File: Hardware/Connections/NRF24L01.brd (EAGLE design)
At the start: 34.3 x 28.9 mm, 9 parts

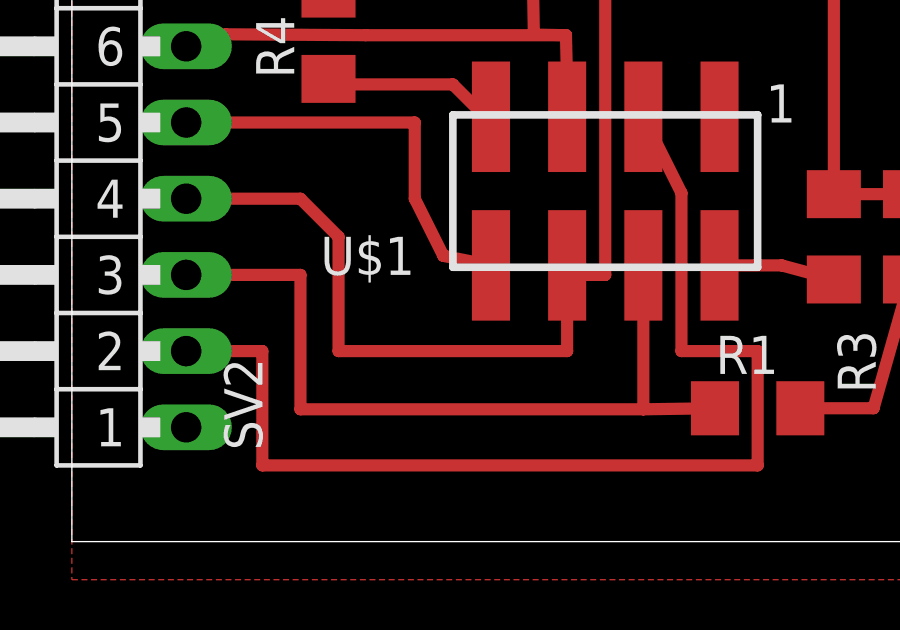
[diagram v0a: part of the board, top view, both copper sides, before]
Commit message: Updated PDF PCB files with Document outline mark. Fixed missing Name for NRF connector. Updated BOM to be correctly formatted.
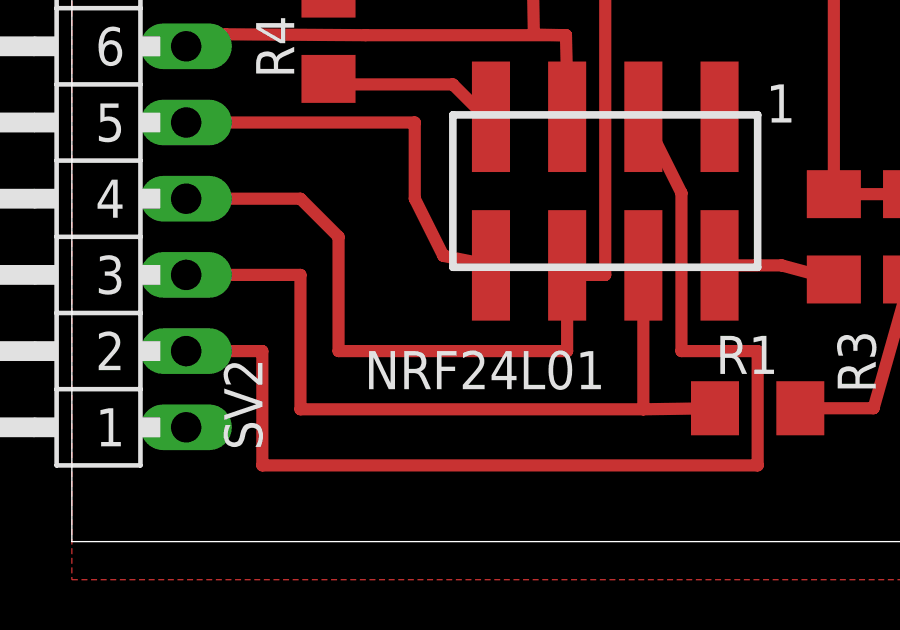
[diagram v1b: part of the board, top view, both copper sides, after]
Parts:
- renumbered U$1 to NRF24L01
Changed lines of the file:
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@@
 <grid distance="0.05" unitdist="inch" unit="mm" style="lines" multiple="1" display="no" altdistance="0.1" altunitdist="mm" altunit="mm"/>
 <layers>
-<layer number="1" name="Top" color="4" fill="1" visible="yes" active="yes"/>
+<layer number="1" name="Top" color="4" fill="1" visible="no" active="yes"/>
 <layer number="2" name="Route2" color="1" fill="3" visible="no" active="no"/>
 <layer number="3" name="Route3" color="4" fill="3" visible="no" active="no"/>
@@
 <layer number="14" name="Route14" color="1" fill="6" visible="no" active="no"/>
 <layer number="15" name="Route15" color="4" fill="6" visible="no" active="no"/>
-<layer number="16" name="Bottom" color="1" fill="1" visible="yes" active="yes"/>
-<layer number="17" name="Pads" color="2" fill="1" visible="yes" active="yes"/>
-<layer number="18" name="Vias" color="2" fill="1" visible="yes" active="yes"/>
-<layer number="19" name="Unrouted" color="6" fill="1" visible="yes" active="yes"/>
+<layer number="16" name="Bottom" color="1" fill="1" visible="no" active="yes"/>
+<layer number="17" name="Pads" color="2" fill="1" visible="no" active="yes"/>
+<layer number="18" name="Vias" color="2" fill="1" visible="no" active="yes"/>
+<layer number="19" name="Unrouted" color="6" fill="1" visible="no" active="yes"/>
 <layer number="20" name="Dimension" color="15" fill="1" visible="yes" active="yes"/>
 <layer number="21" name="tPlace" color="7" fill="1" visible="yes" active="yes"/>
 <layer number="22" name="bPlace" color="7" fill="1" visible="yes" active="yes"/>
-<layer number="23" name="tOrigins" color="15" fill="1" visible="yes" active="yes"/>
-<layer number="24" name="bOrigins" color="15" fill="1" visible="yes" active="yes"/>
+<layer number="23" name="tOrigins" color="15" fill="1" visible="no" active="yes"/>
+<layer number="24" name="bOrigins" color="15" fill="1" visible="no" active="yes"/>
 <layer number="25" name="tNames" color="7" fill="1" visible="yes" active="yes"/>
 <layer number="26" name="bNames" color="7" fill="1" visible="yes" active="yes"/>
 <layer number="27" name="tValues" color="7" fill="1" visible="no" active="yes"/>
 <layer number="28" name="bValues" color="7" fill="1" visible="no" active="yes"/>
-<layer number="29" name="tStop" color="7" fill="3" visible="yes" active="yes"/>
-<layer number="30" name="bStop" color="7" fill="6" visible="yes" active="yes"/>
-<layer number="31" name="tCream" color="7" fill="4" visible="yes" active="yes"/>
-<layer number="32" name="bCream" color="7" fill="5" visible="yes" active="yes"/>
-<layer number="33" name="tFinish" color="6" fill="3" visible="yes" active="yes"/>
-<layer number="34" name="bFinish" color="6" fill="6" visible="yes" active="yes"/>
-<layer number="35" name="tGlue" color="7" fill="4" visible="yes" active="yes"/>
-<layer number="36" name="bGlue" color="7" fill="5" visible="yes" active="yes"/>
-<layer number="37" name="tTest" color="7" fill="1" visible="yes" active="yes"/>
-<layer number="38" name="bTest" color="7" fill="1" visible="yes" active="yes"/>
-<layer number="39" name="tKeepout" color="4" fill="11" visible="yes" active="yes"/>
-<layer number="40" name="bKeepout" color="1" fill="11" visible="yes" active="yes"/>
-<layer number="41" name="tRestrict" color="4" fill="10" visible="yes" active="yes"/>
-<layer number="42" name="bRestrict" color="1" fill="10" visible="yes" active="yes"/>
-<layer number="43" name="vRestrict" color="2" fill="10" visible="yes" active="yes"/>
-<layer number="44" name="Drills" color="7" fill="1" visible="yes" active="yes"/>
-<layer number="45" name="Holes" color="7" fill="1" visible="yes" active="yes"/>
-<layer number="46" name="Milling" color="3" fill="1" visible="yes" active="yes"/>
-<layer number="47" name="Measures" color="7" fill="1" visible="yes" active="yes"/>
-<layer number="48" name="Document" color="7" fill="1" visible="yes" active="yes"/>
-<layer number="49" name="Reference" color="7" fill="1" visible="yes" active="yes"/>
+<layer number="29" name="tStop" color="7" fill="3" visible="no" active="yes"/>
+<layer number="30" name="bStop" color="7" fill="6" visible="no" active="yes"/>
+<layer number="31" name="tCream" color="7" fill="4" visible="no" active="yes"/>
+<layer number="32" name="bCream" color="7" fill="5" visible="no" active="yes"/>
+<layer number="33" name="tFinish" color="6" fill="3" visible="no" active="yes"/>
+<layer number="34" name="bFinish" color="6" fill="6" visible="no" active="yes"/>
+<layer number="35" name="tGlue" color="7" fill="4" visible="no" active="yes"/>
+<layer number="36" name="bGlue" color="7" fill="5" visible="no" active="yes"/>
+<layer number="37" name="tTest" color="7" fill="1" visible="no" active="yes"/>
+<layer number="38" name="bTest" color="7" fill="1" visible="no" active="yes"/>
+<layer number="39" name="tKeepout" color="4" fill="11" visible="no" active="yes"/>
+<layer number="40" name="bKeepout" color="1" fill="11" visible="no" active="yes"/>
+<layer number="41" name="tRestrict" color="4" fill="10" visible="no" active="yes"/>
+<layer number="42" name="bRestrict" color="1" fill="10" visible="no" active="yes"/>
+<layer number="43" name="vRestrict" color="2" fill="10" visible="no" active="yes"/>
+<layer number="44" name="Drills" color="7" fill="1" visible="no" active="yes"/>
+<layer number="45" name="Holes" color="7" fill="1" visible="no" active="yes"/>
+<layer number="46" name="Milling" color="3" fill="1" visible="no" active="yes"/>
+<layer number="47" name="Measures" color="7" fill="1" visible="no" active="yes"/>
+<layer number="48" name="Document" color="7" fill="1" visible="no" active="yes"/>
+<layer number="49" name="Reference" color="7" fill="1" visible="no" active="yes"/>
 <layer number="51" name="tDocu" color="7" fill="1" visible="yes" active="yes"/>
 <layer number="52" name="bDocu" color="7" fill="1" visible="yes" active="yes"/>
@@
 </element>
 <element name="EEPROM" library="eeprom" package="SO8" value="BR25S640FJ-WE2" x="15.24" y="21.59" rot="R270"/>
-<element name="U$1" library="Header" package="TSM-110-XX-XXX-DV" value="2X4SMDHEADER" x="17.78" y="11.43" rot="R180"/>
+<element name="NRF24L01" library="Header" package="TSM-110-XX-XXX-DV" value="2X4SMDHEADER" x="17.78" y="11.43" smashed="yes" rot="R180">
+<attribute name="NAME" x="17.78" y="6.35" size="1.27" layer="25" rot="R180"/>
+<attribute name="VALUE" x="11.43" y="13.97" size="1.27" layer="27" rot="R180"/>
+</element>
 <element name="R1" library="resistor" package="R1206" value="10K" x="22.86" y="4.445"/>
 <element name="R2" library="resistor" package="R1206" value="10K" x="7.62" y="24.765" smashed="yes" rot="R90">
@@
 <signal name="GND">
 <contactref element="SV2" pad="1"/>
-<contactref element="U$1" pad="1"/>
+<contactref element="NRF24L01" pad="1"/>
 <polygon width="0.4064" layer="1" isolate="0.4064">
 <vertex x="0" y="27.94"/>
@@
 <signal name="MOSI">
 <contactref element="EEPROM" pad="5"/>
-<contactref element="U$1" pad="6"/>
+<contactref element="NRF24L01" pad="6"/>
 <wire x1="17.78" y1="19.625" x2="17.84" y2="19.685" width="0.4064" layer="1"/>
 <contactref element="SV2" pad="4"/>
@@
 <signal name="SCK">
 <contactref element="EEPROM" pad="6"/>
-<contactref element="U$1" pad="5"/>
+<contactref element="NRF24L01" pad="5"/>
 <wire x1="16.47" y1="16.88" x2="15.4" y2="16.9" width="0.4064" layer="1"/>
 <wire x1="15.4" y1="16.9" x2="15.34" y2="20.385" width="0.4064" layer="1"/>
@@
 <signal name="CSN_RAD">
 <contactref element="R1" pad="1"/>
-<contactref element="U$1" pad="4"/>
+<contactref element="NRF24L01" pad="4"/>
 <contactref element="SV2" pad="3"/>
 <wire x1="19.05" y1="9.2075" x2="19.05" y2="4.41" width="0.4064" layer="1"/>
@@
 </signal>
 <signal name="CE_RAD">
-<contactref element="U$1" pad="3"/>
+<contactref element="NRF24L01" pad="3"/>
 <contactref element="SV2" pad="2"/>
 <wire x1="3.81" y1="6.35" x2="6.35" y2="6.35" width="0.4064" layer="1"/>
@@
 </signal>
 <signal name="IRQ_RAD">
-<contactref element="U$1" pad="8"/>
+<contactref element="NRF24L01" pad="8"/>
 <contactref element="SV2" pad="5"/>
 <wire x1="3.81" y1="13.97" x2="11.43" y2="13.97" width="0.4064" layer="1"/>
@@
 <signal name="N$2">
 <contactref element="R4" pad="1"/>
-<contactref element="U$1" pad="7"/>
+<contactref element="NRF24L01" pad="7"/>
 <wire x1="13.97" y1="14.1605" x2="13.7795" y2="14.1605" width="0.4064" layer="1"/>
 <wire x1="13.7795" y1="14.1605" x2="12.7" y2="15.24" width="0.4064" layer="1"/>
@@
 </signal>
 <signal name="N$1">
-<contactref element="U$1" pad="2"/>
+<contactref element="NRF24L01" pad="2"/>
 <contactref element="R3" pad="1"/>
 <wire x1="25.4" y1="8.738" x2="23.6605" y2="9.2075" width="0.4064" layer="1"/>

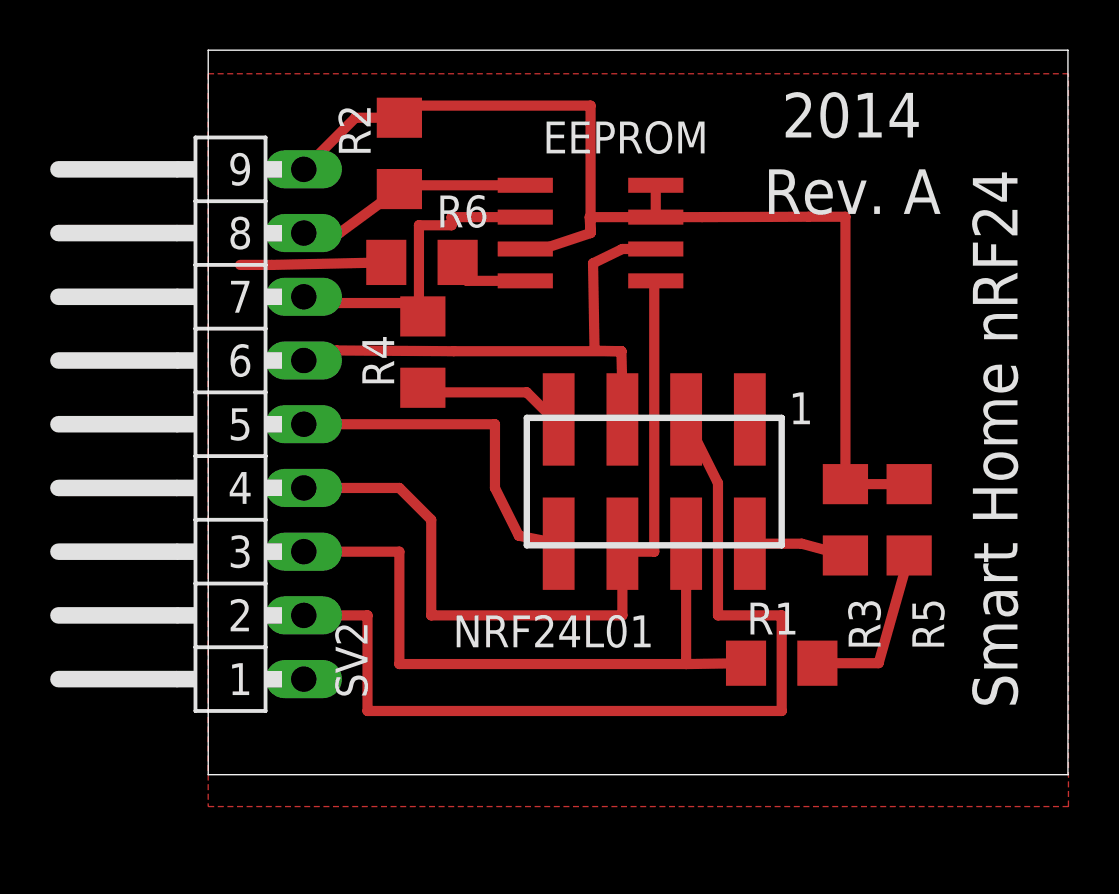
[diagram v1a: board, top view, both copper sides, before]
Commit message: updated pcb design to have reference points
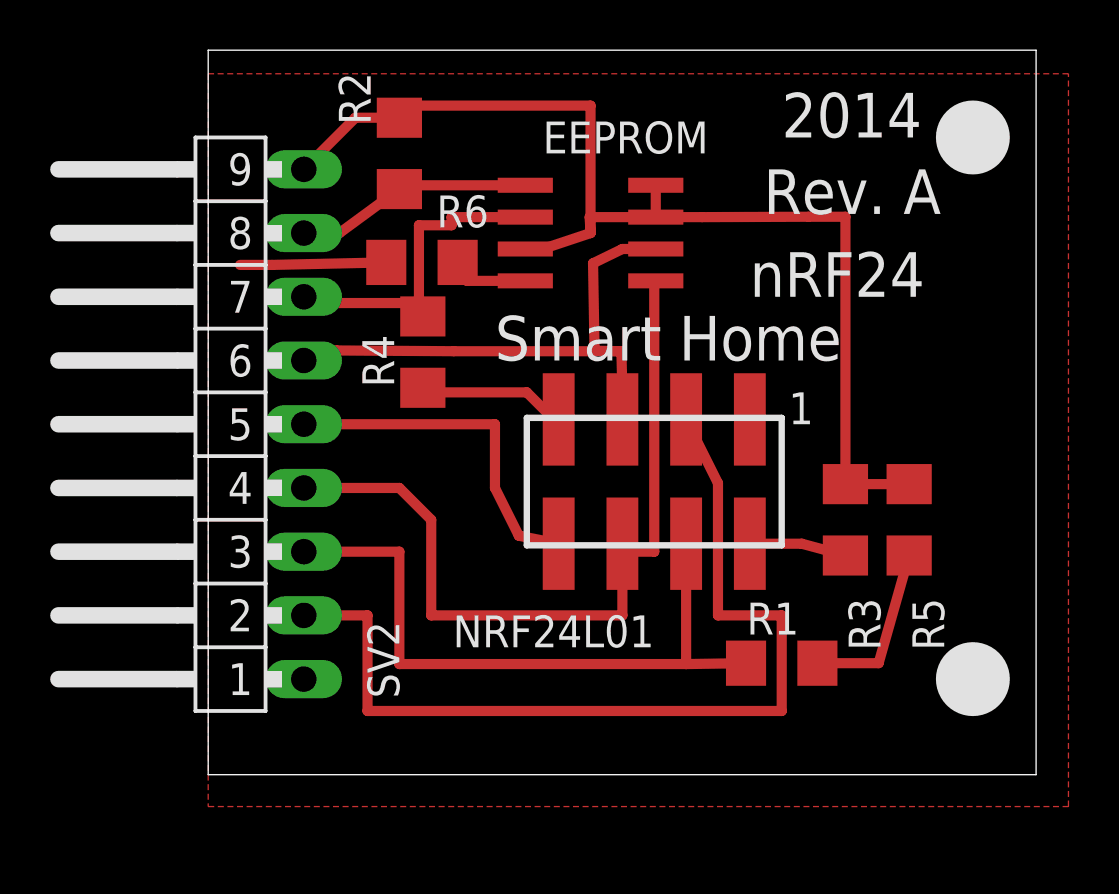
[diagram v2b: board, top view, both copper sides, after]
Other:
- board size 34.3 x 28.9 mm -> 33 x 28.9 mm
- board text added: "Smart Home"
- board text added: "nRF24"
- board text removed: "Smart Home nRF24"
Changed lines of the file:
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@@
 <grid distance="0.05" unitdist="inch" unit="mm" style="lines" multiple="1" display="no" altdistance="0.1" altunitdist="mm" altunit="mm"/>
 <layers>
-<layer number="1" name="Top" color="4" fill="1" visible="no" active="yes"/>
+<layer number="1" name="Top" color="4" fill="1" visible="yes" active="yes"/>
 <layer number="2" name="Route2" color="1" fill="3" visible="no" active="no"/>
 <layer number="3" name="Route3" color="4" fill="3" visible="no" active="no"/>
@@
 <layer number="14" name="Route14" color="1" fill="6" visible="no" active="no"/>
 <layer number="15" name="Route15" color="4" fill="6" visible="no" active="no"/>
-<layer number="16" name="Bottom" color="1" fill="1" visible="no" active="yes"/>
-<layer number="17" name="Pads" color="2" fill="1" visible="no" active="yes"/>
-<layer number="18" name="Vias" color="2" fill="1" visible="no" active="yes"/>
+<layer number="16" name="Bottom" color="1" fill="1" visible="yes" active="yes"/>
+<layer number="17" name="Pads" color="2" fill="1" visible="yes" active="yes"/>
+<layer number="18" name="Vias" color="2" fill="1" visible="yes" active="yes"/>
 <layer number="19" name="Unrouted" color="6" fill="1" visible="no" active="yes"/>
 <layer number="20" name="Dimension" color="15" fill="1" visible="yes" active="yes"/>
@@
 <board>
 <plain>
-<wire x1="0" y1="0" x2="34.27" y2="0" width="0" layer="20"/>
-<wire x1="34.27" y1="0" x2="34.27" y2="28.88" width="0" layer="20"/>
-<wire x1="34.27" y1="28.88" x2="0" y2="28.88" width="0" layer="20"/>
+<wire x1="0" y1="0" x2="33" y2="0" width="0" layer="20"/>
+<wire x1="33" y1="0" x2="33" y2="28.88" width="0" layer="20"/>
+<wire x1="33" y1="28.88" x2="0" y2="28.88" width="0" layer="20"/>
 <wire x1="0" y1="28.88" x2="0" y2="0" width="0" layer="20"/>
-<text x="30.48" y="24.13" size="1.778" layer="21" rot="R270">Smart Home nRF24</text>
 <text x="29.21" y="24.13" size="1.778" layer="21" rot="R180">Rev. A</text>
 <text x="22.86" y="25.4" size="1.778" layer="21">2014</text>
+<polygon width="0.4064" layer="29">
+<vertex x="30.48" y="26.67" curve="-90"/>
+<vertex x="31.75" y="25.4" curve="-90"/>
+<vertex x="30.48" y="24.13" curve="-90"/>
+<vertex x="29.21" y="25.4" curve="-90"/>
+</polygon>
+<polygon width="0.4064" layer="29">
+<vertex x="31.75" y="3.81" curve="90"/>
+<vertex x="30.48" y="5.08" curve="90"/>
+<vertex x="29.21" y="3.81" curve="90"/>
+<vertex x="30.48" y="2.54" curve="90"/>
+</polygon>
+<text x="11.43" y="16.51" size="1.778" layer="21">Smart Home</text>
+<text x="21.59" y="19.05" size="1.778" layer="21">nRF24</text>
+<polygon width="0.4064" layer="21">
+<vertex x="31.75" y="25.4" curve="90"/>
+<vertex x="30.48" y="26.67" curve="90"/>
+<vertex x="29.21" y="25.4" curve="90"/>
+<vertex x="30.48" y="24.13" curve="90"/>
+</polygon>
+<polygon width="0.4064" layer="21">
+<vertex x="31.75" y="3.81" curve="-90"/>
+<vertex x="30.48" y="2.54" curve="-90"/>
+<vertex x="29.21" y="3.81" curve="-90"/>
+<vertex x="30.48" y="5.08" curve="-90"/>
+</polygon>
 </plain>
 <attributes>
@@
 </autorouter>
 <elements>
-<element name="SV2" library="con-lstb" package="MA09-1W" value="CON1" x="3.81" y="13.97" rot="R90">
+<element name="SV2" library="con-lstb" package="MA09-1W" value="CON1" x="3.81" y="13.97" smashed="yes" rot="R90">
 <attribute name="OC_NEWARK" value="unknown" x="25.4" y="39.37" size="1.778" layer="27" rot="R90" display="off"/>
 <attribute name="MPN" value="" x="25.4" y="39.37" size="1.778" layer="27" rot="R90" display="off"/>
 <attribute name="MF" value="" x="25.4" y="39.37" size="1.778" layer="27" rot="R90" display="off"/>
 <attribute name="OC_FARNELL" value="unknown" x="25.4" y="39.37" size="1.778" layer="27" rot="R90" display="off"/>
+<attribute name="NAME" x="7.62" y="3.048" size="1.27" layer="25" ratio="10" rot="R90"/>
+<attribute name="VALUE" x="6.35" y="11.43" size="1.27" layer="27" ratio="10" rot="R90"/>
 </element>
 <element name="EEPROM" library="eeprom" package="SO8" value="BR25S640FJ-WE2" x="15.24" y="21.59" rot="R270"/>
@@
 <element name="R1" library="resistor" package="R1206" value="10K" x="22.86" y="4.445"/>
 <element name="R2" library="resistor" package="R1206" value="10K" x="7.62" y="24.765" smashed="yes" rot="R90">
-<attribute name="NAME" x="6.477" y="24.638" size="1.27" layer="25" rot="R90"/>
+<attribute name="NAME" x="6.477" y="25.908" size="1.27" layer="25" rot="R90"/>
 <attribute name="VALUE" x="10.033" y="23.368" size="1.27" layer="27" rot="R90"/>
 </element>
@@
 <wire x1="10.312" y1="19.685" x2="9.942" y2="20.42" width="0.4064" layer="1"/>
 </signal>
+<signal name="N$5">
+<via x="30.48" y="25.4" extent="1-16" drill="0.6"/>
+</signal>
+<signal name="N$6">
+<via x="30.48" y="3.81" extent="1-16" drill="0.6"/>
+</signal>
 </signals>
